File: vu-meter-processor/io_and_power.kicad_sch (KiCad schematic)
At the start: 14 parts, among them J1 SPI, J2 L, J3 R, J4 +5V, U4 DPU01L-15

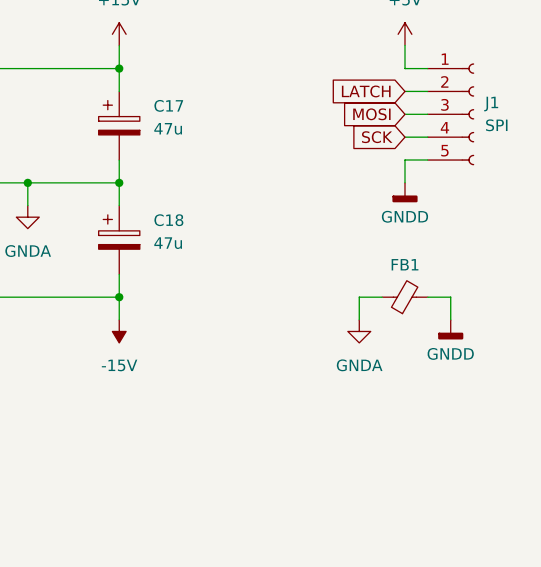
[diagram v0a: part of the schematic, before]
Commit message: fix: change overall power supply to only 5V, make peak detector DNP for now
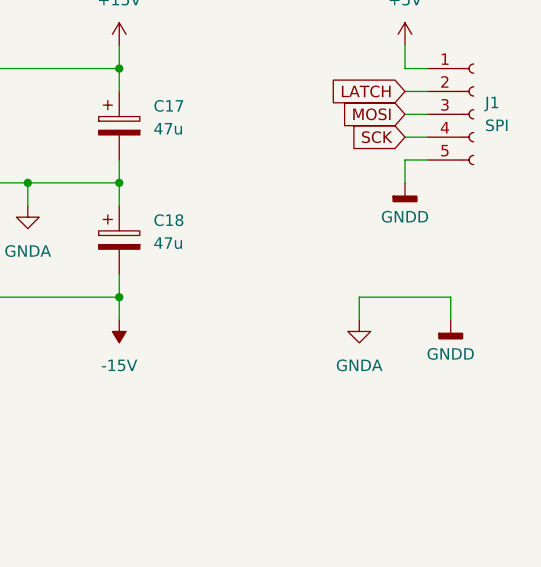
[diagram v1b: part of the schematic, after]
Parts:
- removed FB1: ~, Inductor_SMD:L_0603_1608Metric, symbol Device:FerriteBead_Small
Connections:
- net GNDD is gone; now on net GNDA: C19.2, C20.2, H1.1, H2.1, J1.5 (Pin_5), J4.2 (Pin_2), U4.2 (VIN-)
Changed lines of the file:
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@@
 	(wire
 		(pts
-			(xy 215.9 83.82) (xy 218.44 83.82)
+			(xy 215.9 83.82) (xy 226.06 83.82)
 		)
 		(stroke
@@
 		(pts
 			(xy 143.51 73.66) (xy 146.05 73.66)
-		)
-		(stroke
-			(width 0)
-			(type default)
-		)
-	)
-	(wire
-		(pts
-			(xy 223.52 83.82) (xy 226.06 83.82)
 		)
 		(stroke
@@
 					(unit 1)
 				)
-			)
-		)
-	)
-	(symbol
-		(lib_id "Device:FerriteBead_Small")
-		(at 220.98 83.82 90)
-		(unit 1)
-		(exclude_from_sim no)
-		(in_bom yes)
-		(on_board yes)
-		(dnp no)
-		(property "Reference" "FB1"
-			(at 220.98 80.264 90)
-			(effects
-				(font
-					(size 1.27 1.27)
-				)
-			)
-		)
-		(property "Value" "~"
-			(at 220.9419 80.01 90)
-			(effects
-				(font
-					(size 1.27 1.27)
-				)
-			)
-		)
-		(property "Footprint" "Inductor_SMD:L_0603_1608Metric"
-			(at 220.98 85.598 90)
-			(effects
-				(font
-					(size 1.27 1.27)
-				)
-				(hide yes)
-			)
-		)
-		(property "Datasheet" "~"
-			(at 220.98 83.82 0)
-			(effects
-				(font
-					(size 1.27 1.27)
-				)
-				(hide yes)
-			)
-		)
-		(property "Description" "Ferrite bead, small symbol"
-			(at 220.98 83.82 0)
-			(effects
-				(font
-					(size 1.27 1.27)
-				)
-				(hide yes)
-			)
-		)
-		(pin "1"
-		)
-		(pin "2"
-		)
-		(instances
-			(project ""
-				(path "/50201dbb-ce2c-4681-8d0b-b3063868b684/8588eb71-d238-4a41-a59b-171191caf880"
-					(reference "FB1")
-					(unit 1)
-				)

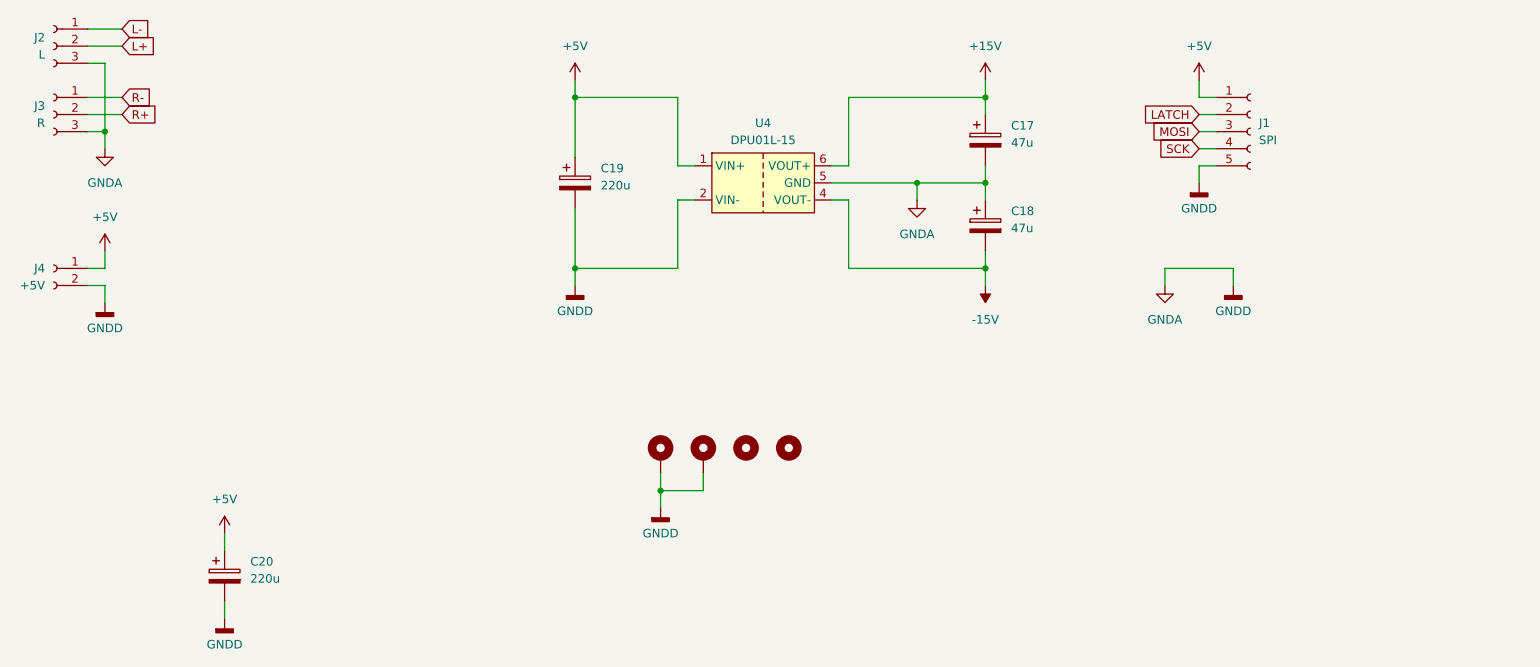
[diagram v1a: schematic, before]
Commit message: remove analog peak detector fully and split one chip into two for better inter-channel performance
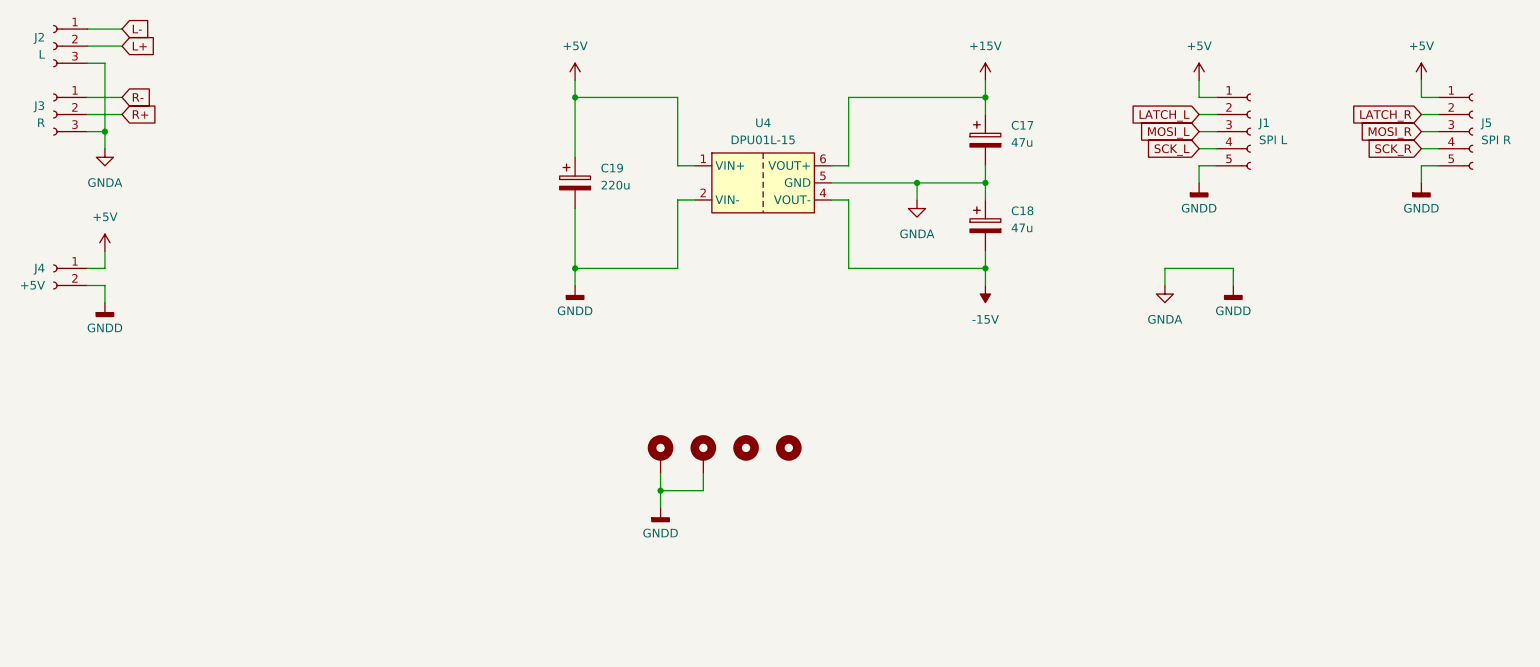
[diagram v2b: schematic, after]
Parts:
- removed C20: 220u, Capacitor_THT:CP_Radial_D8.0mm_P3.50mm, symbol Device:C_Polarized
- added J5: SPI R, Connector_JST:JST_XH_B5B-XH-A_1x05_P2.50mm_Vertical, symbol Connector:Conn_01x05_Socket
- J1: value SPI -> SPI L
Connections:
- net +5V: now also J5.1 (Pin_1)
- net GNDA: now also J5.5 (Pin_5)
- net LATCH renamed LATCH_L
- net MOSI renamed MOSI_L
- net SCK renamed SCK_L
- new net LATCH_R: J5.2 (Pin_2)
- new net MOSI_R: J5.3 (Pin_3)
- new net SCK_R: J5.4 (Pin_4)
